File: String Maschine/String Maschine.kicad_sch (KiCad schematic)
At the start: 37 parts, among them U1 LM358, U2 LM7805_TO220, U3 LM358, U4 LM317_TO-220, U5 MN3209

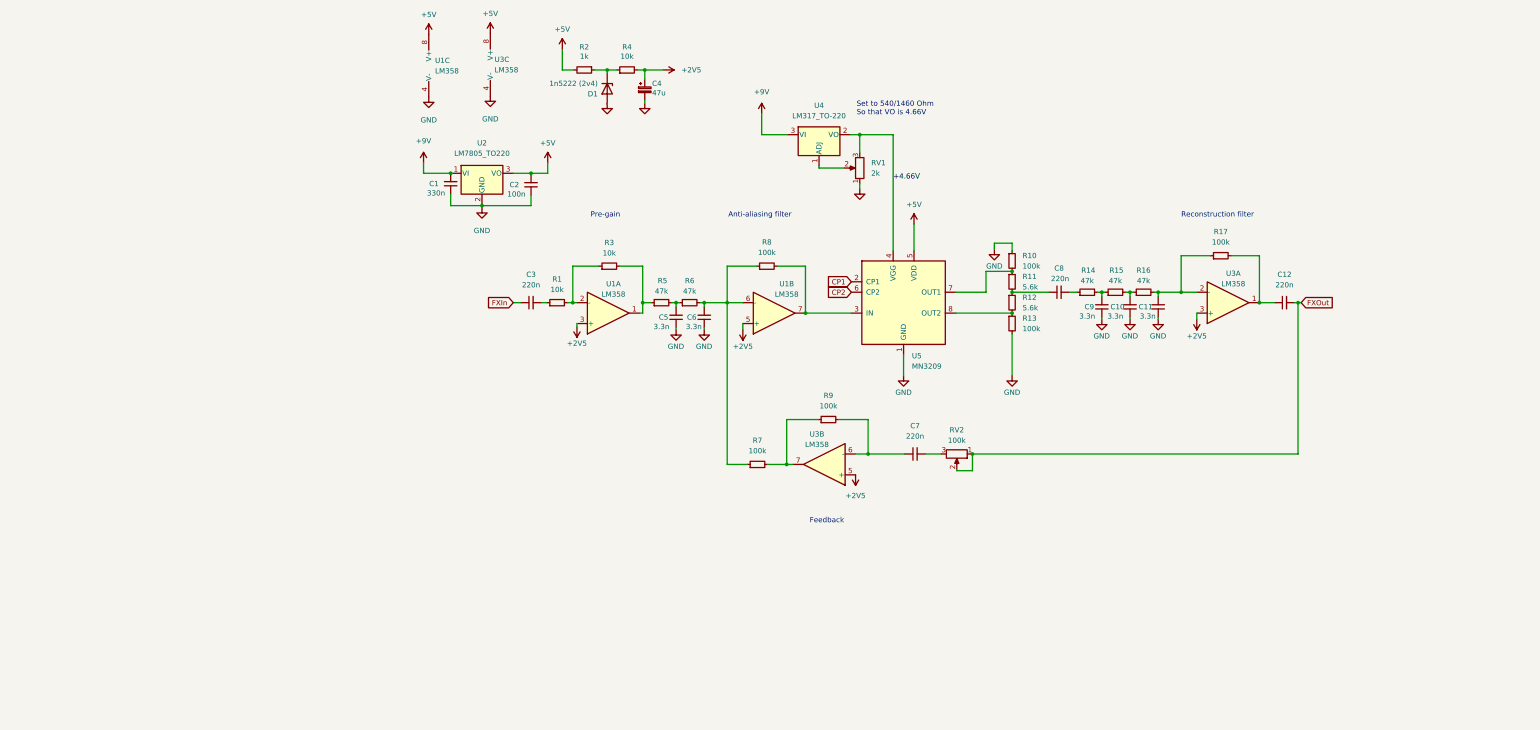
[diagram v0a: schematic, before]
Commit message: Update StringMaschine with level shifters
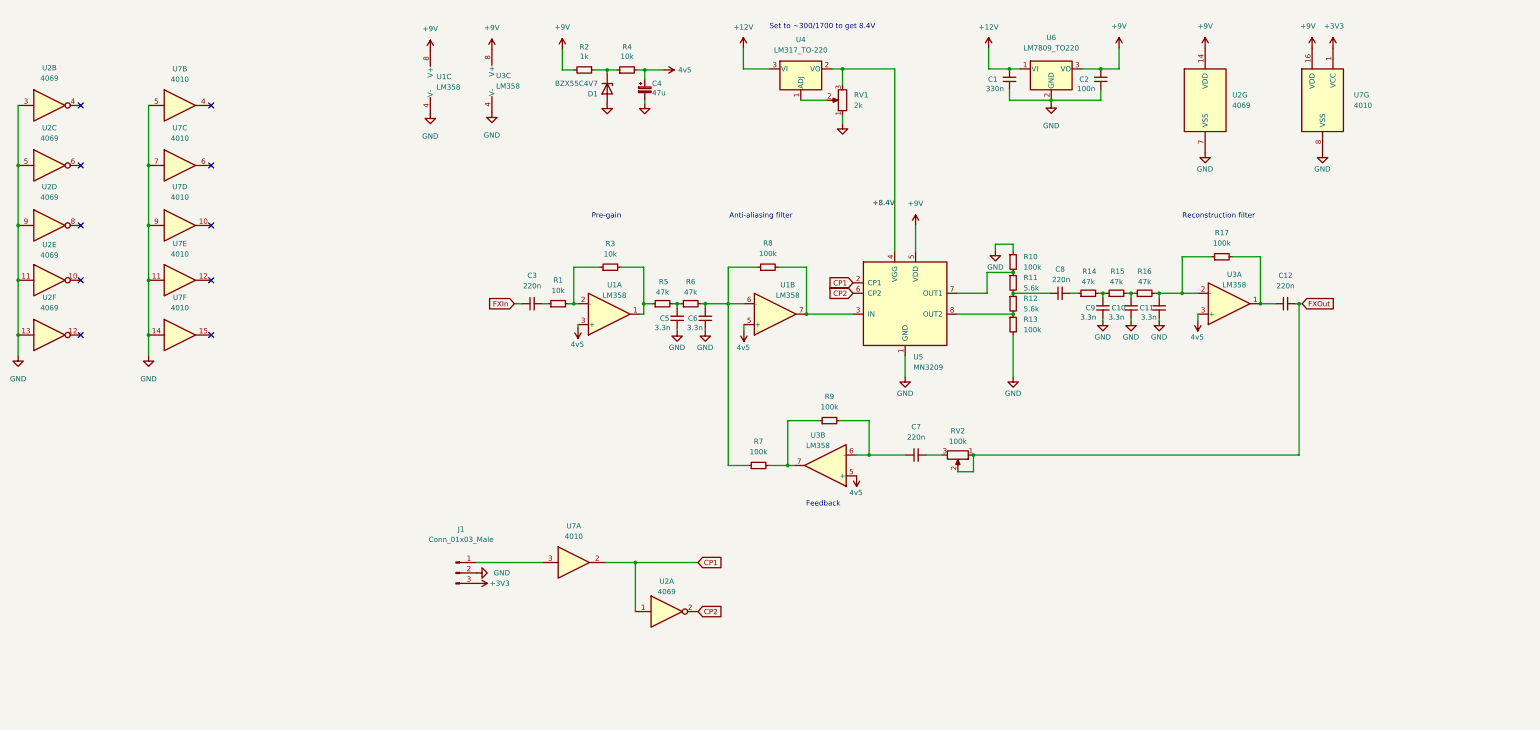
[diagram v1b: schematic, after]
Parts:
- removed U2: LM7805_TO220, Package_TO_SOT_THT:TO-220-3_Vertical, symbol Regulator_Linear:LM7805_TO220
- added J1: Conn_01x03_Male, Connector_PinHeader_2.54mm:PinHeader_1x03_P2.54mm_Vertical, symbol Connector:Conn_01x03_Male
- added U10, U11, U12, U8, U9: 4v5, symbol custom_power:4v5
- added U2: 4069, Package_DIP:DIP-14_W7.62mm, symbol 4xxx:4069
- added U6: LM7809_TO220, Package_TO_SOT_THT:TO-220-3_Vertical, symbol Regulator_Linear:LM7809_TO220
- added U7: 4010, Package_DIP:DIP-16_W10.16mm, symbol 4xxx:4010
- C1, C10, C11, C2, C5, C6, C8, C9: footprint (none) -> Capacitor_THT:C_Rect_L7.0mm_W4.5mm_P5.00mm
- D1: value 1n5222 (2v4) -> BZX55C4V7
- R10, R11, R12, R13, R14, R15, R16, R17, R5, R6, R7, R8, R9, RV1, RV2: footprint (none) -> Resistor_THT:R_Axial_DIN0207_L6.3mm_D2.5mm_P10.16mm_Horizontal
- U1, U3, U5: footprint (none) -> Package_DIP:DIP-8_W7.62mm
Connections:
- net +5V is gone; now on net +9V: C2.2, R2.2, U1.8 (V+), U3.8 (V+), U5.5 (VDD)
- net +9V: now also U2.14 (VDD), U6.3 (VO), U7.16 (VDD); no longer C1.2, U4.3 (VI)
- net CP1: now also U2.1, U7.2
- net CP2: now also U2.2
- net GND: now also J1.2 (Pin_2), U2.11, U2.13, U2.3, U2.5, U2.7 (VSS), U2.9, U6.2 (GND), U7.11, U7.14, U7.5, U7.7, U7.8 (VSS), U7.9
- net +2V5 renamed +4V5
- net +4V5: now also U10.1 (+4V5), U11.1 (+4V5), U12.1 (+4V5), U8.1 (+4V5), U9.1 (+4V5)
- net +4.66V renamed +8.4V 
- new net: J1.1 (Pin_1), U7.3
- new net +12V: C1.2, U4.3 (VI), U6.1 (VI)
- new net +3V3: J1.3 (Pin_3), U7.1 (VCC)
- no-connect marks 0 -> 10
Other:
- note added: "Set to ~300/1700 to get 8.4V"
- note removed: "Set to 540/1460 Ohm So that VO is 4.66V"
- moved on the sheet: C1, C2, RV1, U1C, U3C, U4

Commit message: Add opamp rail splitter
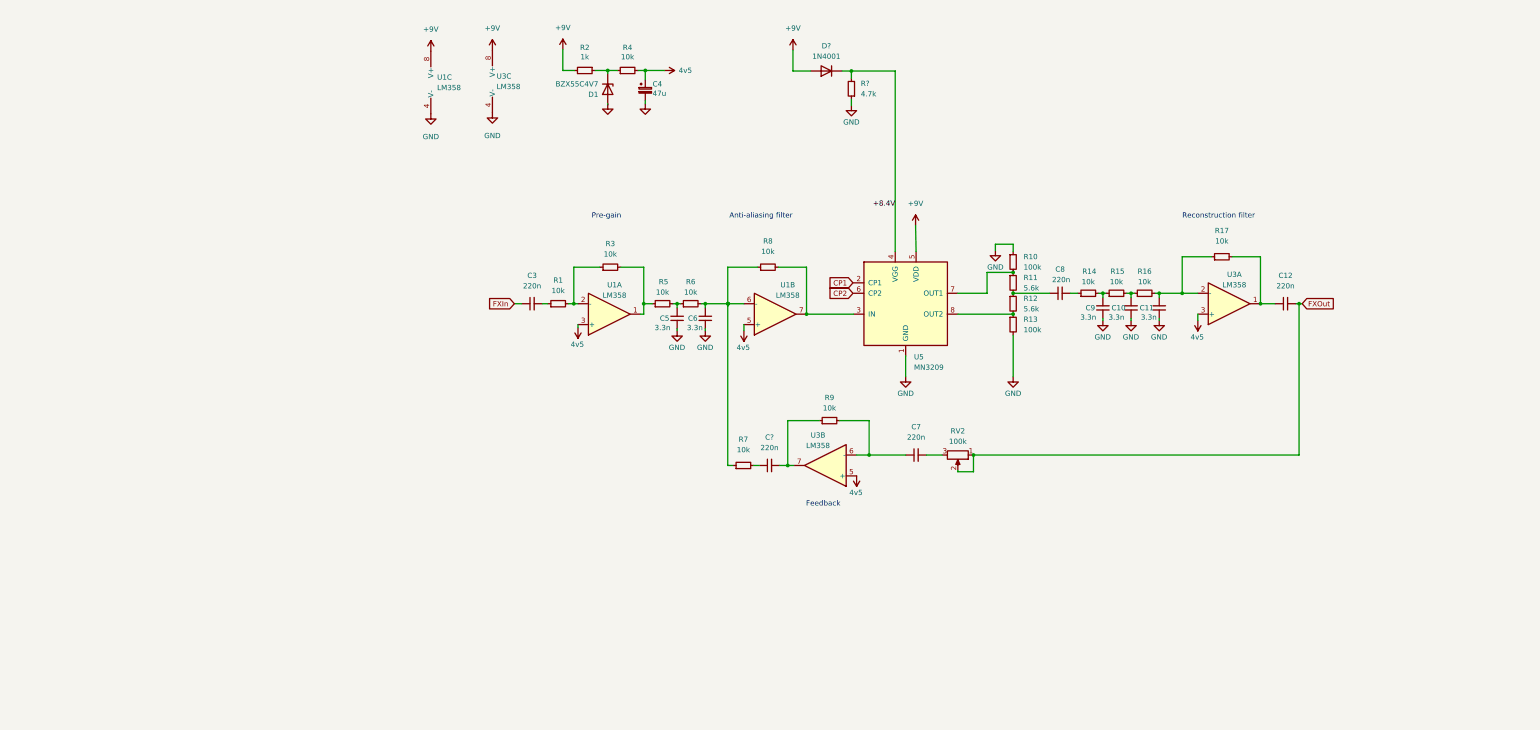
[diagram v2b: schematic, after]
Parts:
- removed C1: 330n, Capacitor_THT:C_Rect_L7.0mm_W4.5mm_P5.00mm, symbol Device:C_Small
- removed C2: 100n, Capacitor_THT:C_Rect_L7.0mm_W4.5mm_P5.00mm, symbol Device:C_Small
- removed J1: Conn_01x03_Male, Connector_PinHeader_2.54mm:PinHeader_1x03_P2.54mm_Vertical, symbol Connector:Conn_01x03_Male
- removed RV1: 2k, Resistor_THT:R_Axial_DIN0207_L6.3mm_D2.5mm_P10.16mm_Horizontal, symbol Device:R_Potentiometer
- removed U2: 4069, Package_DIP:DIP-14_W7.62mm, symbol 4xxx:4069
- removed U4: LM317_TO-220, Package_TO_SOT_THT:TO-220-3_Vertical, symbol Regulator_Linear:LM317_TO-220
- removed U6: LM7809_TO220, Package_TO_SOT_THT:TO-220-3_Vertical, symbol Regulator_Linear:LM7809_TO220
- removed U7: 4010, Package_DIP:DIP-16_W10.16mm, symbol 4xxx:4010
- added C?: 220n, Capacitor_THT:C_Rect_L7.0mm_W4.5mm_P5.00mm, symbol Device:C_Small
- added D?: 1N4001, Diode_THT:D_DO-41_SOD81_P10.16mm_Horizontal, symbol Diode:1N4001
- added R?: 4.7k, Resistor_THT:R_Axial_DIN0207_L6.3mm_D2.5mm_P10.16mm_Horizontal, symbol Device:R_Small
- R14, R15, R16, R5, R6: value 47k -> 10k
- R17, R7, R8, R9: value 100k -> 10k
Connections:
- net +8.4V : now also D?.1 (K), R?.2
- net +9V: now also D?.2 (A)
- net CP1: no longer U5.2 (CP1)
- net CP2: no longer U5.6 (CP2)
- net GND: now also R?.1
- net at R9.1, U3.7: now also C?.2; no longer R7.2
- new net: C?.1, R7.2
- no-connect marks 10 -> 0
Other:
- note removed: "Set to ~300/1700 to get 8.4V"
- moved on the sheet: R7

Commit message: Adapt the keytar to use VCA
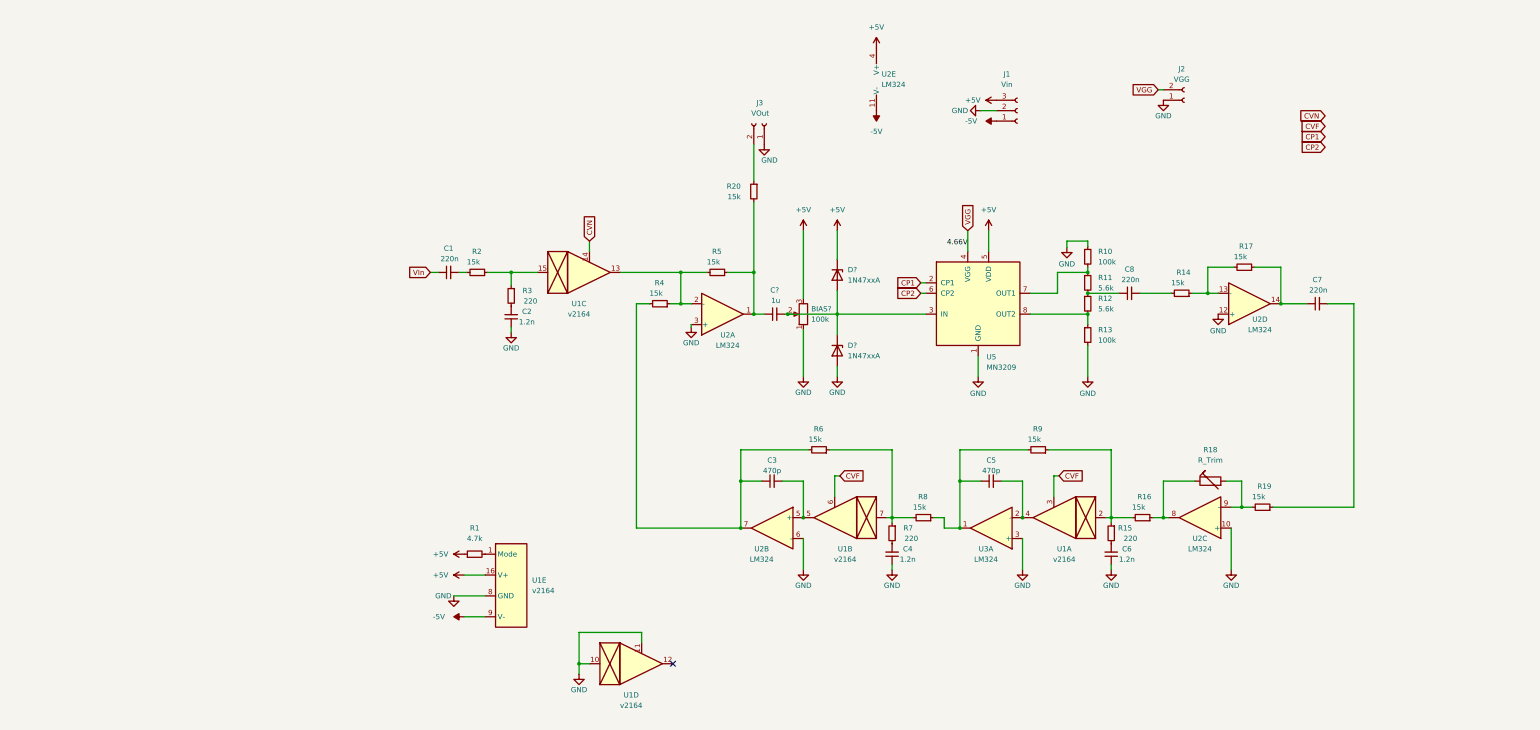
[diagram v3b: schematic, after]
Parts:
- removed C10, C11, C9: 3.3n, Capacitor_THT:C_Rect_L7.0mm_W4.5mm_P5.00mm, symbol Device:C_Small
- removed C12, C?: 220n, Capacitor_THT:C_Rect_L7.0mm_W4.5mm_P5.00mm, symbol Device:C_Small
- removed C4: 47u, Capacitor_THT:CP_Radial_D5.0mm_P2.00mm, symbol Device:C_Polarized_Small
- removed D1: BZX55C4V7, Diode_THT:D_DO-35_SOD27_P7.62mm_Horizontal, symbol Device:D_Zener
- removed D?: 1N4001, Diode_THT:D_DO-41_SOD81_P10.16mm_Horizontal, symbol Diode:1N4001
- removed R?: 4.7k, Resistor_THT:R_Axial_DIN0207_L6.3mm_D2.5mm_P10.16mm_Horizontal, symbol Device:R_Small
- removed RV2: 100k, Resistor_THT:R_Axial_DIN0207_L6.3mm_D2.5mm_P10.16mm_Horizontal, symbol Device:R_Potentiometer
- removed U1, U3: LM358, Package_DIP:DIP-8_W7.62mm, symbol Amplifier_Operational:LM358
- removed U10, U11, U12, U8, U9: 4v5, symbol custom_power:4v5
- added BIAS?: 100k, symbol Device:R_Potentiometer
- added C1: 220n, Capacitor_THT:C_Rect_L7.0mm_W4.5mm_P5.00mm, symbol Device:C_Small
- added C2, C4: 1.2n, Capacitor_THT:C_Rect_L7.0mm_W4.5mm_P5.00mm, symbol Device:C_Small
- added C?: 1u, Capacitor_THT:C_Rect_L7.0mm_W4.5mm_P5.00mm, symbol Device:C_Small
- added D? (x2): 1N47xxA, Diode_THT:D_DO-41_SOD81_P10.16mm_Horizontal, symbol Diode:1N47xxA
- added J1: Vin, symbol Connector:Conn_01x03_Female
- added J2: VGG, symbol Connector:Conn_01x02_Female
- added J3: VOut, symbol Connector:Conn_01x02_Female
- added R18: R_Trim, symbol Device:R_Trim
- added R19, R20: 15k, Resistor_THT:R_Axial_DIN0207_L6.3mm_D2.5mm_P10.16mm_Horizontal, symbol Device:R_Small
- added U1: v2164, symbol coolaudio:v2164
- added U2, U3: LM324, symbol Amplifier_Operational:LM324
- C3: value 220n -> 470p
- C5: value 3.3n -> 470p
- C6: value 3.3n -> 1.2n
- R1: value 10k -> 4.7k
- R14, R16, R17, R4, R5, R6, R8, R9: value 10k -> 15k
- R15, R3, R7: value 10k -> 220
- R2: value 1k -> 15k
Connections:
- net FXIn is gone; now on an unnamed net: C3.1
- net CP1: now also U5.2 (CP1)
- net CP2: now also U5.6 (CP2)
- net GND: now also BIAS?.1, C2.1, C4.1, D?.2 (A), J1.2 (Pin_2), J2.1 (Pin_1), J3.1 (Pin_1), U1.10, U1.11, U1.8 (GND), U2.10 (+), U2.12 (+), U2.3 (+), U2.6 (-), U3.3 (+); no longer C5.1
- net at R9.1: now also R15.1, R16.2, U1.2
- net at R9.2: now also C5.1, R8.1, U3.1; no longer C7.1
- net at C7.2: now also R19.1
- net at R4.1: now also R5.2, U1.13, U2.2 (-); no longer R2.1
- net at U5.3 (IN): now also BIAS?.2, C?.2, D?.1 (K), D?.2 (A); no longer R8.2
- net at C3.2: now also U1.5, U2.5 (+); no longer R1.1
- net at R3.2: now also C2.2; no longer R5.1
- net at R17.1: now also C7.1, U2.14; no longer R16.2
- net at R14.2: now also C8.2; no longer R15.1
- net at R7.2: now also C4.2
- net at R3.1: now also R2.1, U1.15; no longer R1.2
- net at R16.1: now also R18.1, U2.8; no longer R15.2
- net at R14.1: now also R17.2, U2.13 (-); no longer C8.2
- net +4V5: no longer names the net of R4.2
- net +4V5: now also R6.2, U2.7
- net +8.4V  renamed VGG
- net VGG: now also J2.2 (Pin_2)
- net +9V: no longer names the net of R2.2
- net +9V: now also C1.2; no longer U5.5 (VDD)
- new net: C5.2, U1.4, U3.2 (-)
- new net: R18.2, R19.2, U2.9 (-)
- new net: C6.2, R15.2
- new net: J3.2 (Pin_2), R20.1
- new net: R6.1, R7.1, R8.2, U1.7
- new net: C?.1, R20.2, R5.1, U2.1
- new net: R1.2, U1.1 (Mode)
- new net +5V: BIAS?.3, D?.1 (K), J1.3 (Pin_3), R1.1, U1.16 (V+), U2.4 (V+), U5.5 (VDD)
- new net -5V: J1.1 (Pin_1), U1.9 (V-), U2.11 (V-)
- new net CVF: U1.3, U1.6
- new net CVN: U1.14
- new net VIn: C1.1
- no-connect marks 0 -> 1
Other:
- note removed: "Anti-aliasing filter"
- note removed: "Feedback"
- note removed: "Pre-gain"
- note removed: "Reconstruction filter"
- moved on the sheet: C8, R10, R11, R12, R13, U5

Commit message: Strin Maschine - first revision before review
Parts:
- removed R1: 4.7k, Resistor_THT:R_Axial_DIN0207_L6.3mm_D2.5mm_P10.16mm_Horizontal, symbol Device:R_Small
- removed R17, R19: 15k, Resistor_THT:R_Axial_DIN0207_L6.3mm_D2.5mm_P10.16mm_Horizontal, symbol Device:R_Small
- removed R18: R_Trim, symbol Device:R_Trim
- removed U3: LM324, symbol Amplifier_Operational:LM324
- added FBACK1, VNOISE1: 100k, symbol Device:R_Potentiometer
- added J4: Vin, symbol Connector:Conn_01x03_Female
- added J5: CTLS, symbol Connector:Conn_01x04_Female
- added SW1, SW3: FBACK, symbol Switch:SW_SPST
- added SW2: NOISE, symbol Switch:SW_SPST
- added TP1: NIn, symbol Connector:TestPoint
- added TP10: DELAY, symbol Connector:TestPoint
- added TP2: VCF, symbol Connector:TestPoint
- added TP3: VGG, symbol Connector:TestPoint
- added TP4: VBIAS, symbol Connector:TestPoint
- added TP5: CP2, symbol Connector:TestPoint
- added TP6: CP1, symbol Connector:TestPoint
- added TP7: CVF, symbol Connector:TestPoint
- added TP8: CVN, symbol Connector:TestPoint
- added TP9: GND, symbol Connector:TestPoint
- added U3: Pentanoise, symbol coolaudio:Pentanoise
- C2, C4, C6: value 1.2n -> 560p
- R14, R16, R2, R4, R5, R6, R8, R9: value 15k -> 27k
- R15, R3, R7: value 220 -> 470
- R20: value 15k -> 10k
- gave numbers to parts that had none: 4
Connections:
- net +5V: now also J4.3 (Pin_3), U3.1 (5V)
- net -5V: now also J4.1 (Pin_1)
- net CP1: now also J5.3 (Pin_3), TP5.1
- net CP2: now also J5.4 (Pin_4), TP6.1
- net CVF: now also J5.2 (Pin_2), TP7.1
- net CVN: now also J5.1 (Pin_1), TP8.1
- net GND: now also U2.5 (+), J4.2 (Pin_2), TP9.1, U3.8 (GND), VNOISE1.3; no longer U2.6 (-)
- net VGG: now also TP3.1
- net at BIAS1.2, C9.2, D1.2 (A)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: now also TP4.1
- net at C5.1, R8.1, R9.2: now also U2.1
- net at C5.2, U1.4: now also U2.2 (-)
- net at R16.1: now also SW3.1 (A); no longer U2.8
- net at U2.9 (-): now also R4.1, R5.2, SW2.2 (B)
- net at C7.1, U2.14: now also FBACK1.1, FBACK1.2
- net at C7.2: now also SW3.2 (B), TP10.1
- net at R2.1, R3.1, U1.15: now also TP1.1
- net at R14.1, U2.13 (-): now also FBACK1.3
- net at C9.1, R20.2, R5.1: now also U2.8; no longer U2.1
- net at C3.2, U1.5: now also U2.6 (-); no longer U2.5 (+)
- net at C3.1, R6.2, U2.7: now also SW1.1 (A), TP2.1; no longer R4.2
- net VIn: no longer names the net of C1.1
- net VIn: now also VNOISE1.2
- new net: SW2.1 (A), U1.13
- new net: U3.7 (Out1), VNOISE1.1
- new net: R4.2, SW1.2 (B)
- no-connect marks 1 -> 6
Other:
- note added: "-(filtered feedback + excitation)"
- note added: "256 BBD Delay 12.8ms @ 10kHz, 0.25ms @ 200kHz (40Hz at 20kHz clock to 4kHz at 200kHz)"
- note added: "Class AB"
- note added: "Excitation Keep NIn at <1Vp-p for low distortion"
- note added: "Feedback To be replaced with VCA"
- note added: "Must be 14/15 Vin 4.66Vgg for 5Vin"
- note added: "Set Vbias to ~2.5V"
- note added: "VCF 6dB/dec, 0-20kHz Vin at -0.33V to 3.3V"
- moved on the sheet: BIAS1, C1, C2, C3, C4, C5, C6, C7, C8, C9, D1, D2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

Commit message: String Maschine - assign symbols
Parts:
- BIAS1, VNOISE1: footprint (none) -> Potentiometer_THT:Potentiometer_Bourns_3266Y_Vertical
- FBACK1: footprint (none) -> Connector_JST:JST_PH_B3B-PH-K_1x03_P2.00mm_Vertical
- J1, J4: footprint (none) -> Connector_PinHeader_2.54mm:PinHeader_1x03_P2.54mm_Vertical
- J2, J3, SW1, SW2, SW3: footprint (none) -> Connector_PinHeader_2.54mm:PinHeader_1x02_P2.54mm_Vertical
- J5: footprint (none) -> Connector_PinHeader_2.54mm:PinHeader_1x04_P2.54mm_Vertical
- TP1, TP10, TP2, TP3, TP4, TP5, TP6, TP7, TP8, TP9: footprint (none) -> TestPoint:TestPoint_Pad_D1.0mm
- U1: footprint (none) -> Package_DIP:DIP-16_W7.62mm
- U2: footprint (none) -> Package_DIP:DIP-14_W7.62mm
- U3: footprint (none) -> Package_DIP:DIP-8_W7.62mm

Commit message: String Maschine - fix VCF range
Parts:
- C3, C5: value 470p -> 1.2n
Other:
- note added: "VCF 6dB/dec, 0-15kHz Vin at -0.33V to 3.3V"
- note removed: "VCF 6dB/dec, 0-20kHz Vin at -0.33V to 3.3V"
- moved on the sheet: U1D, U1E
